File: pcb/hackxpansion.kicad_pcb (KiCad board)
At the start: 2 copper layers, 51 parts, among them IC1 ADS7128IRTET, J1 Conn_01x03_MountingPin, J3 USB_C_Receptacle_USB2.0_14P, J4 USB_C_Receptacle_USB2.0_14P, Q1 BSS138, Q2 2N7002, SW1 SW_Push, SW2 SW_Push, SW25 SW_On_Off, U12 BQ24075RGT, U2 RP2354B, U7 SPX3819M5-L-3-3, Y1 ABM8-272-T3

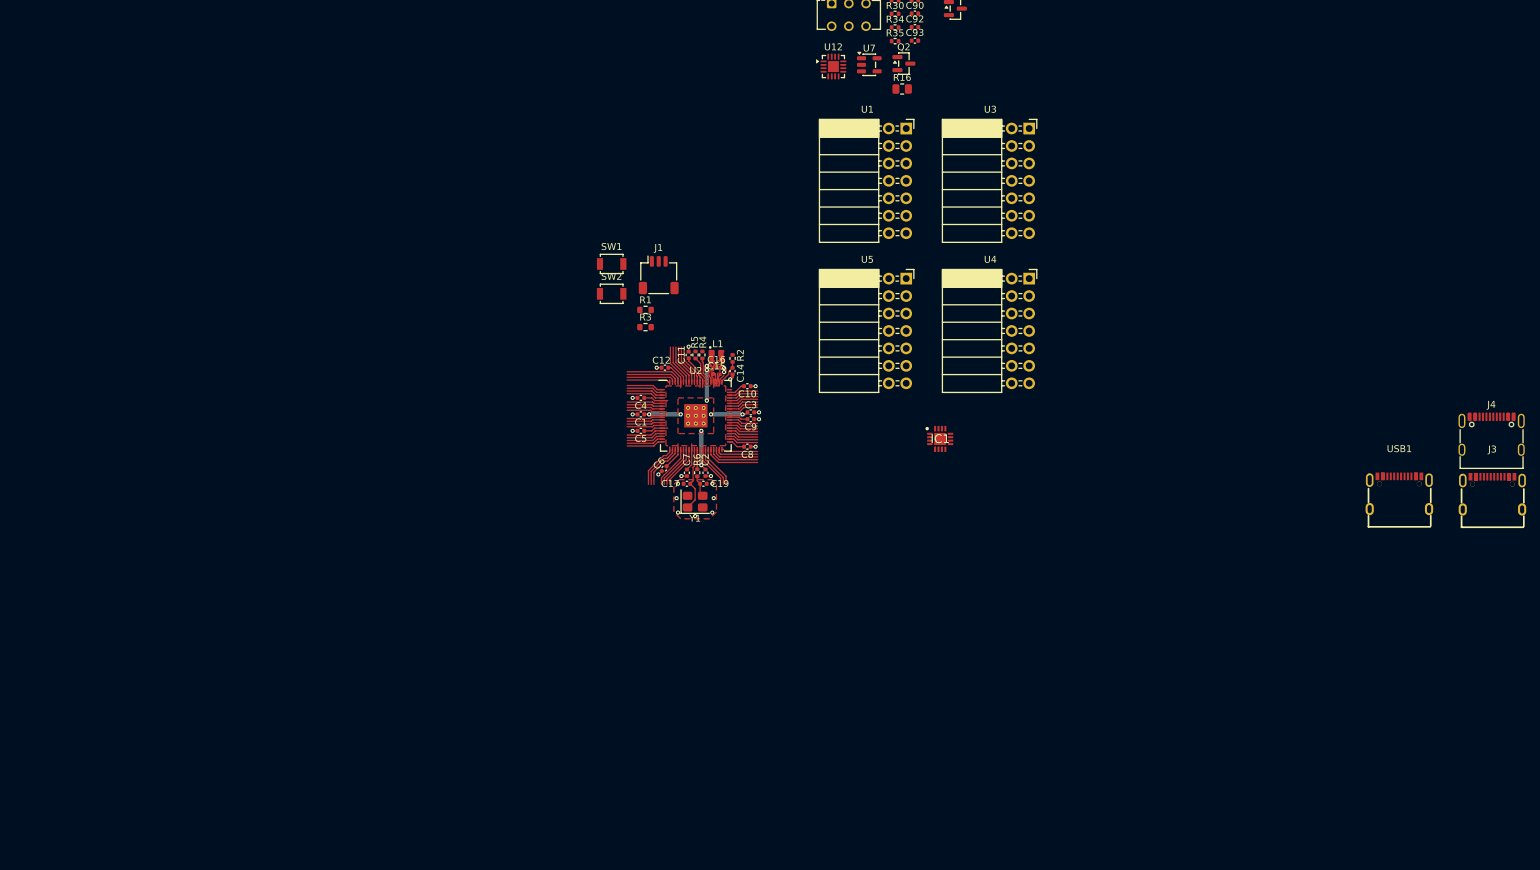
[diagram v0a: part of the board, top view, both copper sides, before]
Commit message: switched to pico blade connectors
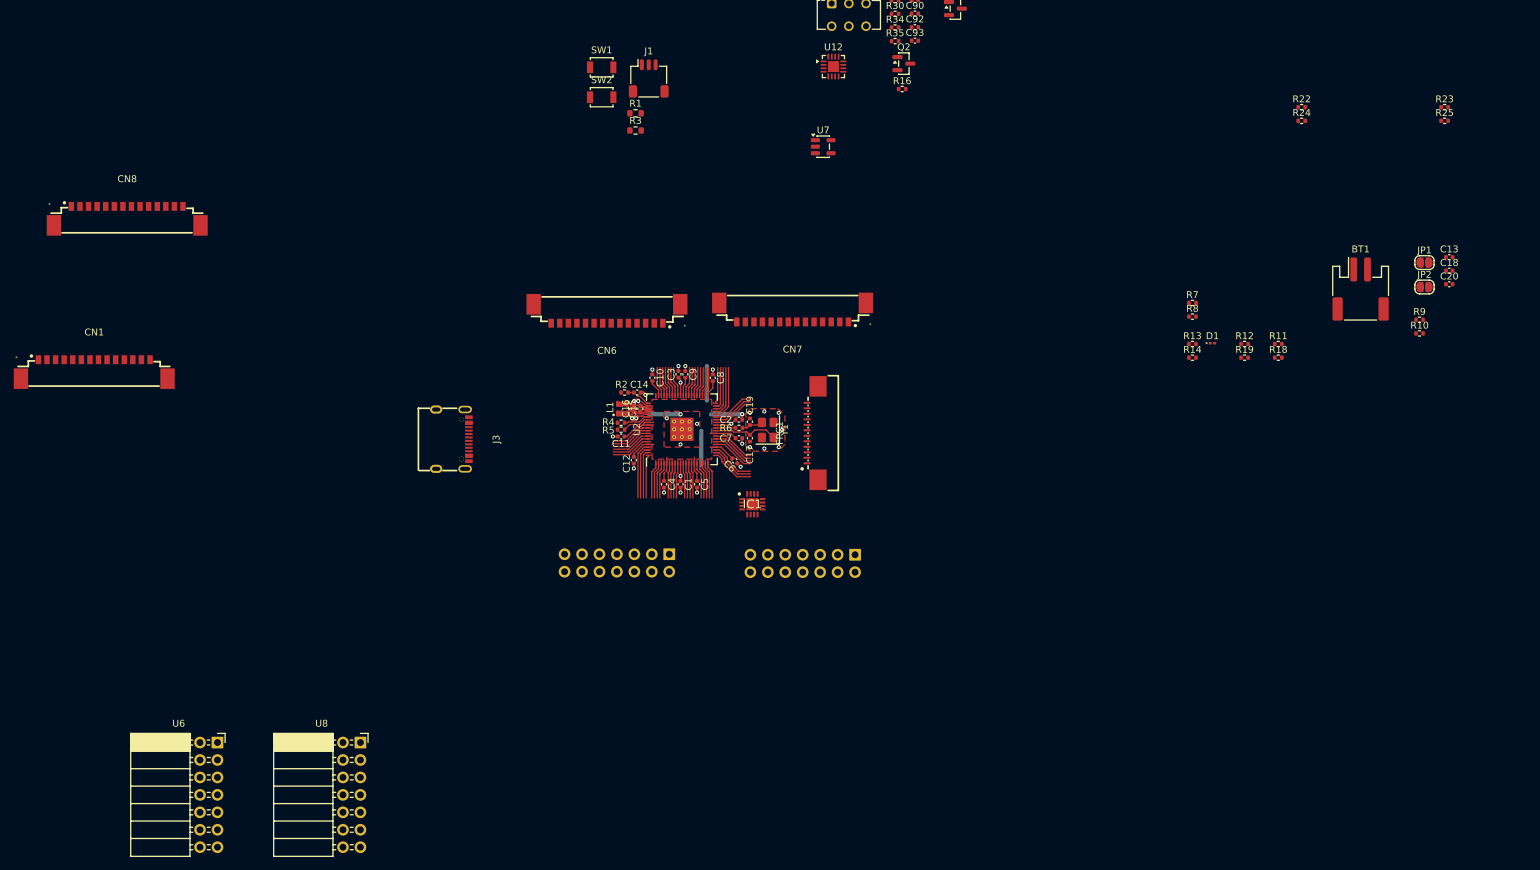
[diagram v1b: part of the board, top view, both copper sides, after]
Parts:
- removed J4: USB_C_Receptacle_USB2.0_14P, Connector_USB:USB_C_Receptacle_G-Switch_GT-USB-7010ASV
- removed U4, U5: ~, Connector_PinSocket_2.54mm:PinSocket_2x07_P2.54mm_Horizontal
- removed USB1: TYPE-C 16PIN 2MD, easyeda2kicad:USB-C-SMD_TYPE-C-16PIN-2MD-073
- added BT1: Battery_Cell, Connector_JST:JST_PH_S2B-PH-SM4-TB_1x02-1MP_P2.00mm_Horizontal, F.Cu at (225.8, 66.6)
- added C13: 1u, Capacitor_SMD:C_0402_1005Metric, F.Cu at (238.7, 61.9)
- added C18: 1u, Capacitor_SMD:C_0402_1005Metric, F.Cu at (238.7, 63.9)
- added C20: 1u, Capacitor_SMD:C_0402_1005Metric, F.Cu at (238.7, 65.9)
- added CN1: 533981471, easyeda2kicad:CONN-SMD_14P-P1.25_MOLEX_533981471, F.Cu at (41.4, 78.2)
- added CN6: 533981471, easyeda2kicad:CONN-SMD_14P-P1.25_MOLEX_533981471, F.Cu at (116.1, 70.2)
- added CN7: 533981471, easyeda2kicad:CONN-SMD_14P-P1.25_MOLEX_533981471, F.Cu at (143.1, 70.0)
- added CN8: 533981471, easyeda2kicad:CONN-SMD_14P-P1.25_MOLEX_533981471, F.Cu at (46.2, 55.9)
- added D1: LED, LED_SMD:LED_0201_0603Metric, F.Cu at (204.2, 74.4)
- added FPC1: AFC08-S12ECA-00, easyeda2kicad:FPC-SMD_AFC08-S12ECA-00, F.Cu at (146.0, 87.5)
- added JP1: SolderJumper_2_Open, Jumper:SolderJumper-2_P1.3mm_Open_RoundedPad1.0x1.5mm, F.Cu at (235.1, 62.7)
- added JP2: SolderJumper_2_Open, Jumper:SolderJumper-2_P1.3mm_Open_RoundedPad1.0x1.5mm, F.Cu at (235.1, 66.3)
- added R10: 5k1, Resistor_SMD:R_0402_1005Metric, F.Cu at (234.4, 73.0)
- added R11: 10K, Resistor_SMD:R_0402_1005Metric, F.Cu at (213.8, 74.6)
- added R12: 10K, Resistor_SMD:R_0402_1005Metric, F.Cu at (208.9, 74.6)
- added R13: 100R, Resistor_SMD:R_0402_1005Metric, F.Cu at (201.3, 74.6)
- added R14: 10k, Resistor_SMD:R_0402_1005Metric, F.Cu at (201.3, 76.5)
- added R18: 10K, Resistor_SMD:R_0402_1005Metric, F.Cu at (213.8, 76.5)
- added R19: 10K, Resistor_SMD:R_0402_1005Metric, F.Cu at (208.9, 76.5)
- added R22: 10K, Resistor_SMD:R_0402_1005Metric, F.Cu at (217.2, 40.1)
- added R23: 10K, Resistor_SMD:R_0402_1005Metric, F.Cu at (238.0, 40.1)
- added R24: 10K, Resistor_SMD:R_0402_1005Metric, F.Cu at (217.2, 42.1)
- added R25: 10K, Resistor_SMD:R_0402_1005Metric, F.Cu at (238.0, 42.1)
- added R7: 10, Resistor_SMD:R_0402_1005Metric, F.Cu at (201.3, 68.6)
- added R8: 10k, Resistor_SMD:R_0402_1005Metric, F.Cu at (201.3, 70.6)
- added R9: 5k1, Resistor_SMD:R_0402_1005Metric, F.Cu at (234.4, 71.0)
- added U6: ~, Connector_PinSocket_2.54mm:PinSocket_2x07_P2.54mm_Horizontal, F.Cu at (59.4, 132.6)
- added U8: ~, Connector_PinSocket_2.54mm:PinSocket_2x07_P2.54mm_Horizontal, F.Cu at (80.2, 132.6)
- C15, C16: footprint RP2354B_MINIMAL:C_0402_1005Metric_small_pads -> Capacitor_SMD:C_0402_1005Metric
- R16: footprint Resistor_SMD:R_0805_2012Metric -> Resistor_SMD:R_0402_1005Metric
- U1, U3: moved to B.Cu
- moved J3 151.6 mm to (93.6, 88.4), turned to -90 degrees
- moved U1 70.9 mm to (125.1, 105.2), turned to 90 degrees
- moved U3 67.0 mm to (152.2, 105.2), turned to 90 degrees
- moved IC1 28.9 mm to (137.2, 97.9)
- moved J1 28.7 mm to (122.1, 35.9)
- moved R1 28.7 mm to (120.2, 41.0)
- moved SW1 28.7 mm to (115.3, 34.3)
- moved SW2 28.7 mm to (115.3, 38.6)
- moved R3 28.7 mm to (120.2, 43.5)
- moved R2 16.5 mm to (118.6, 81.6), turned to 0 degrees
- moved L1 15.7 mm to (118.3, 84.0), turned to 90 degrees
- moved C11 15.4 mm to (118.1, 88.0), turned to 180 degrees
- moved R4 15.4 mm to (118.1, 86.0), turned to 0 degrees
- moved R5 15.3 mm to (118.1, 87.0), turned to 0 degrees
- moved Y1 14.8 mm to (139.5, 87.1), turned to 90 degrees
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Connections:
- net /ADC/i2c0.SCL renamed /Main Board/ADC/i2c0.SCL
- net /ADC/i2c0.SDA renamed /Main Board/ADC/i2c0.SDA
- net /Power/+BATT renamed /Main Board/Power/+BATT
- net /Power/ILIM renamed /Main Board/Power/ILIM
- net /Power/ISET renamed /Main Board/Power/ISET
- net /Power/REG-OUT renamed /Main Board/Power/REG-OUT
- net /Power/SYSOFF renamed /Main Board/Power/SYSOFF
- net /Power/TS renamed /Main Board/Power/TS
- net /Power/VSW renamed /Main Board/Power/VSW
- net /RP2354B/GPIO14 renamed /Main Board/ADC/SCL
- net /RP2354B/GPIO15 renamed /Main Board/ADC/SDA
- net /RP2354B/GPIO34 renamed /Main Board/RP2354B/spi.SCLK
- net /RP2354B/GPIO35 renamed /Main Board/RP2354B/spi.MOSI
- net /RP2354B/QSPI_SS renamed /Main Board/RP2354B/QSPI_SS
- net /RP2354B/RUN renamed /Main Board/RP2354B/RUN
- net /RP2354B/SWCLK renamed /Main Board/RP2354B/SWCLK
- net /RP2354B/SWDIO renamed /Main Board/RP2354B/SWDIO
- net /RP2354B/~{USB_BOOT} renamed /Main Board/RP2354B/~{USB_BOOT}
- C1 pad 2: GND -> /GND
- C10 pad 1: +3V3 -> /+3V3
- C10 pad 2: GND -> /GND
- C11 pad 1: +3V3 -> /+3V3
- C11 pad 2: GND -> /GND
- C12 pad 1: +3V3 -> /+3V3
- C12 pad 2: GND -> /GND
- C14 pad 2: GND -> /GND
- C15 pad 1: +3V3 -> /+3V3
- C15 pad 2: GND -> /GND
- C16 pad 2: GND -> /GND
- C17 pad 1: GND -> /GND
- C19 pad 1: GND -> /GND
- C2 pad 2: GND -> /GND
- C3 pad 2: GND -> /GND
- C4 pad 1: +3V3 -> /+3V3
- C4 pad 2: GND -> /GND
- C5 pad 1: +3V3 -> /+3V3
- C5 pad 2: GND -> /GND
- C6 pad 1: +3V3 -> /+3V3
- C6 pad 2: GND -> /GND
- C7 pad 1: +3V3 -> /+3V3
- C7 pad 2: GND -> /GND
- C8 pad 1: +3V3 -> /+3V3
- C8 pad 2: GND -> /GND
- C88 pad 1: GND -> /Main Board/Power/GND
- C88 pad 2: VBUS -> /Main Board/Power/VBUS
- C9 pad 1: +3V3 -> /+3V3
- C9 pad 2: GND -> /GND
- C90 pad 1: GND -> /Main Board/Power/GND
- C92 pad 1: GND -> /Main Board/Power/GND
- C93 pad 1: GND -> /Main Board/Power/GND
- C93 pad 2: /Power/3V3 -> /+3V3
- IC1 pad 1: /ADC/mod1.MD0 -> /Main Board/ADC/mod1.MD0
- IC1 pad 10: +3V3 -> /+3V3
- IC1 pad 12: /ADC/ALERT -> /Main Board/ADC/ALERT
- IC1 pad 15: /ADC/mod0.MD0 -> /Main Board/ADC/mod0.MD0
- IC1 pad 16: /ADC/mod0.MD1 -> /Main Board/ADC/mod0.MD1
- IC1 pad 17: GND -> /GND
- IC1 pad 2: /ADC/mod1.MD1 -> /Main Board/ADC/mod1.MD1
- IC1 pad 3: /ADC/mod2.MD0 -> /Connector Main Mod2/mod.MD0
- IC1 pad 4: /ADC/mod2.MD1 -> /Connector Main Mod2/mod.MD1
- IC1 pad 5: /ADC/mod3.MD0 -> /Connector Main Mod3/mod.MD0
- IC1 pad 6: /ADC/mod3.MD1 -> /Connector Main Mod3/mod.MD1
- IC1 pad 7: +3V3 -> /+3V3
- IC1 pad 9: GND -> /GND
- J1 pad 2: GND -> /GND
- J1 pad MP: GND -> /GND
- J3 pad A1: GND -> /GND
- J3 pad A12: GND -> /GND
- J3 pad A4: /USB/VBUS -> /Main Board/Power/VBUS
- J3 pad A5: /USB/CC1 -> /Main Board/USB/CC1
- J3 pad A6: /USB/D+ -> /Main Board/RP2354B/D+
- J3 pad A7: /USB/D- -> /Main Board/RP2354B/D-
- J3 pad A9: /USB/VBUS -> /Main Board/Power/VBUS
- J3 pad B1: GND -> /GND
- J3 pad B12: GND -> /GND
- J3 pad B4: /USB/VBUS -> /Main Board/Power/VBUS
- J3 pad B5: /USB/CC2 -> /Main Board/USB/CC2
- J3 pad B6: /USB/D+ -> /Main Board/RP2354B/D+
- J3 pad B7: /USB/D- -> /Main Board/RP2354B/D-
- J3 pad B9: /USB/VBUS -> /Main Board/Power/VBUS
- Q1 pad 1: /Display/BACKLIGHT -> /Main Board/Display/BACKLIGHT
- Q1 pad 2: GND -> /GND
- Q2 pad 2: GND -> /Main Board/Power/GND
- R2 pad 1: +3V3 -> /+3V3
- R28 pad 2: GND -> /Main Board/Power/GND
- R30 pad 2: GND -> /Main Board/Power/GND
- R34 pad 2: GND -> /Main Board/Power/GND
- R4 pad 1: /RP2354B/D- -> /Main Board/RP2354B/D-
- R5 pad 1: /RP2354B/D+ -> /Main Board/RP2354B/D+
- SW1 pad 1: GND -> /GND
- SW2 pad 1: GND -> /GND
- SW25 pad 1: GND -> /Main Board/Power/GND
- U1 pad 1: GND -> /GND
- U1 pad 10: /Module Bay 0/GPIO5 -> /Main Board/Module Bay 0/GPIO5
- U1 pad 11: /Module Bay 0/GPIO6 -> /Main Board/Module Bay 0/GPIO6
- U1 pad 12: /Module Bay 0/GPIO7 -> /Main Board/Module Bay 0/GPIO7
- U1 pad 13: /Module Bay 0/GPIO8 -> /Main Board/Module Bay 0/GPIO8
- U1 pad 14: /Module Bay 0/GPIO9 -> /Main Board/Module Bay 0/GPIO9
- U1 pad 2: +3V3 -> /+3V3
- U1 pad 3: /Module Bay 0/mod.MD0 -> /Main Board/ADC/mod0.MD0
- U1 pad 4: /Module Bay 0/mod.MD1 -> /Main Board/ADC/mod0.MD1
- U1 pad 5: /Module Bay 0/GPIO0 -> /Main Board/Module Bay 0/GPIO0
- U1 pad 6: /Module Bay 0/GPIO1 -> /Main Board/Module Bay 0/GPIO1
- U1 pad 7: /Module Bay 0/GPIO2 -> /Main Board/Module Bay 0/GPIO2
- U1 pad 8: /Module Bay 0/GPIO3 -> /Main Board/Module Bay 0/GPIO3
- U1 pad 9: /Module Bay 0/GPIO4 -> /Main Board/Module Bay 0/GPIO4
- U12 pad 13: VBUS -> /Main Board/Power/VBUS
- U12 pad 17: GND -> /Main Board/Power/GND
- U12 pad 4: GND -> /Main Board/Power/GND
- U12 pad 5: GND -> /Main Board/Power/GND
- U12 pad 8: GND -> /Main Board/Power/GND
- U2 pad 1: /RP2354B/GPIO4 -> /Main Board/Module Bay 0/GPIO3
- U2 pad 11: /RP2354B/GPIO12 -> /Main Board/Module Bay 1/GPIO3
- U2 pad 12: /RP2354B/GPIO13 -> /Main Board/Module Bay 1/GPIO0
- U2 pad 15: +3V3 -> /+3V3
- U2 pad 16: /RP2354B/GPIO16 -> /Main Board/Module Bay 1/GPIO1
- U2 pad 17: /RP2354B/GPIO17 -> /Main Board/Module Bay 1/GPIO9
- U2 pad 18: /RP2354B/GPIO18 -> /Connector Main Mod2/bank.GPIO1
- U2 pad 19: /RP2354B/GPIO19 -> /Connector Main Mod2/bank.GPIO0
- U2 pad 2: /RP2354B/GPIO5 -> /Main Board/ADC/ALERT
- U2 pad 20: /RP2354B/GPIO20 -> /Main Board/Module Bay 1/GPIO5
- U2 pad 21: /RP2354B/GPIO21 -> /Main Board/Module Bay 1/GPIO6
- U2 pad 22: /RP2354B/GPIO22 -> /Connector Main Mod2/bank.GPIO2
- U2 pad 23: /RP2354B/GPIO23 -> /Connector Main Mod2/bank.GPIO4
- U2 pad 24: +3V3 -> /+3V3
- U2 pad 25: /RP2354B/GPIO24 -> /Connector Main Mod3/bank.GPIO3
- U2 pad 26: /RP2354B/GPIO25 -> /Main Board/Display/DC
- U2 pad 27: /RP2354B/GPIO26 -> /Connector Main Mod2/bank.GPIO9
- U2 pad 28: /RP2354B/GPIO27 -> /Connector Main Mod3/bank.GPIO4
- U2 pad 29: +3V3 -> /+3V3
- U2 pad 3: /RP2354B/GPIO6 -> /Main Board/Module Bay 0/GPIO1
- U2 pad 36: /RP2354B/GPIO28 -> /Connector Main Mod2/bank.GPIO5
- U2 pad 37: /RP2354B/GPIO29 -> /Connector Main Mod2/bank.GPIO6
- U2 pad 38: /RP2354B/GPIO30 -> /Connector Main Mod3/bank.GPIO2
- U2 pad 39: /RP2354B/GPIO31 -> /Main Board/Display/BACKLIGHT
- U2 pad 4: /RP2354B/GPIO7 -> /Main Board/Module Bay 0/GPIO0
- U2 pad 40: /RP2354B/GPIO32 -> /Connector Main Mod2/bank.GPIO3
- U2 pad 41: +3V3 -> /+3V3
- U2 pad 42: /RP2354B/GPIO33 -> /Main Board/Module Bay 0/GPIO9
- U2 pad 45: /RP2354B/GPIO36 -> /Connector Main Mod3/bank.GPIO1
- U2 pad 46: /RP2354B/GPIO37 -> /Connector Main Mod3/bank.GPIO0
- U2 pad 47: /RP2354B/GPIO38 -> /Main Board/Display/CS
- U2 pad 48: /RP2354B/GPIO39 -> /Connector Main Mod3/bank.GPIO9
- U2 pad 49: /RP2354B/GPIO40 -> /Main Board/Module Bay 0/GPIO7
- U2 pad 5: +3V3 -> /+3V3
- U2 pad 50: +3V3 -> /+3V3
- U2 pad 52: /RP2354B/GPIO41 -> /Main Board/Module Bay 0/GPIO8
- U2 pad 53: /RP2354B/GPIO42 -> /Main Board/Module Bay 1/GPIO7
- U2 pad 54: /RP2354B/GPIO43 -> /Main Board/Module Bay 1/GPIO8
- U2 pad 55: /RP2354B/GPIO44 -> /Connector Main Mod2/bank.GPIO7
- U2 pad 56: /RP2354B/GPIO45 -> /Connector Main Mod2/bank.GPIO8
- U2 pad 57: /RP2354B/GPIO46 -> /Connector Main Mod3/bank.GPIO7
- U2 pad 58: /RP2354B/GPIO47 -> /Connector Main Mod3/bank.GPIO8
- U2 pad 59: +3V3 -> /+3V3
- U2 pad 6: /RP2354B/GPIO8 -> /Connector Main Mod3/bank.GPIO6
- U2 pad 60: +3V3 -> /+3V3
- U2 pad 62: GND -> /GND
- U2 pad 64: +3V3 -> /+3V3
- U2 pad 68: +3V3 -> /+3V3
- U2 pad 69: +3V3 -> /+3V3
- U2 pad 7: /RP2354B/GPIO9 -> /Connector Main Mod3/bank.GPIO5
- U2 pad 70: /RP2354B/QSPI_SD3 -> unconnected-(U2-QSPI_SD3-Pad70)
- U2 pad 71: /RP2354B/QSPI_SCLK -> unconnected-(U2-QSPI_SCLK-Pad71)
- U2 pad 72: /RP2354B/QSPI_SD0 -> /Main Board/Display/RESET
- U2 pad 73: /RP2354B/QSPI_SD2 -> unconnected-(U2-QSPI_SD2-Pad73)
- U2 pad 74: /RP2354B/QSPI_SD1 -> unconnected-(U2-QSPI_SD1-Pad74)
- U2 pad 76: +3V3 -> /+3V3
- U2 pad 77: /RP2354B/GPIO0 -> /Main Board/Module Bay 0/GPIO5
- U2 pad 78: /RP2354B/GPIO1 -> /Main Board/Module Bay 0/GPIO6
- U2 pad 79: /RP2354B/GPIO2 -> /Main Board/Module Bay 0/GPIO2
- U2 pad 8: /RP2354B/GPIO10 -> /Main Board/Module Bay 1/GPIO2
- U2 pad 80: /RP2354B/GPIO3 -> /Main Board/Module Bay 0/GPIO4
- U2 pad 81: GND -> /GND
- U2 pad 9: /RP2354B/GPIO11 -> /Main Board/Module Bay 1/GPIO4
- U3 pad 1: GND -> /GND
- U3 pad 10: /Module Bay 1/GPIO5 -> /Main Board/Module Bay 1/GPIO5
- U3 pad 11: /Module Bay 1/GPIO6 -> /Main Board/Module Bay 1/GPIO6
- U3 pad 12: /Module Bay 1/GPIO7 -> /Main Board/Module Bay 1/GPIO7
- U3 pad 13: /Module Bay 1/GPIO8 -> /Main Board/Module Bay 1/GPIO8
- U3 pad 14: /Module Bay 1/GPIO9 -> /Main Board/Module Bay 1/GPIO9
- U3 pad 2: +3V3 -> /+3V3
- U3 pad 3: /Module Bay 1/mod.MD0 -> /Main Board/ADC/mod1.MD0
- U3 pad 4: /Module Bay 1/mod.MD1 -> /Main Board/ADC/mod1.MD1
- U3 pad 5: /Module Bay 1/GPIO0 -> /Main Board/Module Bay 1/GPIO0
- U3 pad 6: /Module Bay 1/GPIO1 -> /Main Board/Module Bay 1/GPIO1
- U3 pad 7: /Module Bay 1/GPIO2 -> /Main Board/Module Bay 1/GPIO2
- U3 pad 8: /Module Bay 1/GPIO3 -> /Main Board/Module Bay 1/GPIO3
- U3 pad 9: /Module Bay 1/GPIO4 -> /Main Board/Module Bay 1/GPIO4
- U7 pad 2: GND -> /Main Board/Power/GND
- U7 pad 5: /Power/3V3 -> /+3V3
- Y1 pad 2: GND -> /GND
- Y1 pad 4: GND -> /GND
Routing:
- net +3V3: track 34.3 -> 0.00 mm
- net /+3V3: track 0.00 -> 34.3 mm
- net /GND: track 0.00 -> 14.3 mm, vias 0 -> 13
- net GND: track 9.67 -> 0.00 mm, vias 22 -> 0
- net /RP2354B/GPIO0: track 8.38 -> 0.00 mm
- net /Main Board/Module Bay 0/GPIO5: track 0.00 -> 8.38 mm
- net /RP2354B/GPIO28: track 8.06 -> 0.00 mm
- net /Connector Main Mod2/bank.GPIO5: track 0.00 -> 8.06 mm
- net /RP2354B/GPIO1: track 7.75 -> 0.00 mm
- net /Main Board/Module Bay 0/GPIO6: track 0.00 -> 7.75 mm
- net /RP2354B/GPIO29: track 7.43 -> 0.00 mm
- net /Connector Main Mod2/bank.GPIO6: track 0.00 -> 7.43 mm
- net /RP2354B/GPIO2: track 7.12 -> 0.00 mm
- net /Main Board/Module Bay 0/GPIO2: track 0.00 -> 7.12 mm
- net /RP2354B/GPIO30: track 6.81 -> 0.00 mm
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- added copper zone on F.Cu, net (none)
- removed copper zone on F.Cu, net +3V3
- removed copper zone on F.Cu, net GND

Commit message: reanottad stuff
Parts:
- removed C88, C90, C92, C93: 4u7, Capacitor_SMD:C_0402_1005Metric
- removed CN6, CN7, CN8: 533981471, easyeda2kicad:CONN-SMD_14P-P1.25_MOLEX_533981471
- removed J3: USB_C_Receptacle_USB2.0_14P, easyeda2kicad:USB-C-SMD_TYPE-C-16PIN-2MD-073
- removed R28: 3k9, Resistor_SMD:R_0402_1005Metric
- removed R30: 1k5, Resistor_SMD:R_0402_1005Metric
- removed R34, R35: 10k, Resistor_SMD:R_0402_1005Metric
- removed SW25: SW_On_Off, Button_Switch_THT:SW_CK_JS202011AQN_DPDT_Angled
- removed U12: BQ24075RGT, Package_DFN_QFN:VQFN-16-1EP_3x3mm_P0.5mm_EP1.6x1.6mm
- removed U8: ~, Connector_PinSocket_2.54mm:PinSocket_2x07_P2.54mm_Horizontal
- added C21: 4u7, Capacitor_SMD:C_0402_1005Metric, F.Cu at (94.2, 39.3)
- added C22: 4u7, Capacitor_SMD:C_0402_1005Metric, F.Cu at (94.2, 41.2)
- added C23: 4u7, Capacitor_SMD:C_0402_1005Metric, F.Cu at (94.2, 43.2)
- added C24: 4u7, Capacitor_SMD:C_0402_1005Metric, F.Cu at (94.2, 45.2)
- added CN2: 533981471, easyeda2kicad:CONN-SMD_14P-P1.25_MOLEX_533981471, F.Cu at (86.5, 78.9)
- added CN3: 533981471, easyeda2kicad:CONN-SMD_14P-P1.25_MOLEX_533981471, F.Cu at (86.5, 62.8)
- added CN4: 533981471, easyeda2kicad:CONN-SMD_14P-P1.25_MOLEX_533981471, F.Cu at (86.5, 70.8)
- added J2: USB_C_Receptacle_USB2.0_14P, easyeda2kicad:USB-C-SMD_TYPE-C-16PIN-2MD-073, F.Cu at (66.9, 63.6)
- added R15: 100k, Resistor_SMD:R_0402_1005Metric, F.Cu at (88.9, 47.3)
- added R17: 10K, Resistor_SMD:R_0402_1005Metric, F.Cu at (62.9, 72.2)
- added R20: 10K, Resistor_SMD:R_0402_1005Metric, F.Cu at (78.8, 39.3)
- added R21: 10K, Resistor_SMD:R_0402_1005Metric, F.Cu at (67.8, 72.2)
- added SW3: SW_On_Off, Button_Switch_THT:SW_CK_JS202011AQN_DPDT_Angled, F.Cu at (85.0, 39.8)
- added U4: ~, Connector_PinSocket_2.54mm:PinSocket_2x07_P2.54mm_Horizontal, F.Cu at (75.1, 40.6)
- added U5: SPX3819M5-L-3-3, Package_TO_SOT_SMD:SOT-23-5, F.Cu at (84.8, 48.7)
- R16: value 100k -> 10K
- R22: value 10K -> 3k9
- R23: value 10K -> 1k5
- R24, R25: value 10K -> 10k
- U7: value SPX3819M5-L-3-3 -> BQ24075RGT; footprint Package_TO_SOT_SMD:SOT-23-5 -> Package_DFN_QFN:VQFN-16-1EP_3x3mm_P0.5mm_EP1.6x1.6mm
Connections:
- FPC1 pad 13: /GND -> unconnected-(FPC1-Pad13)
- FPC1 pad 14: /GND -> unconnected-(FPC1-Pad14)
- R16 pad 1: /Main Board/Power/+BATT -> /Main Board/ADC/mod0.MD1
- R16 pad 2: Net-(SW25A-C) -> /GND
- R18 pad 1: /Main Board/ADC/mod0.MD1 -> /Connector Daughter Mod2/mod.MD1
- R19 pad 1: /Main Board/ADC/mod1.MD1 -> /Connector Daughter Mod3/mod.MD1
- R22 pad 1: /Connector Daughter Mod2/mod.MD1 -> /Main Board/Power/ISET
- R22 pad 2: /GND -> /Main Board/Power/GND
- R23 pad 1: /Connector Daughter Mod3/mod.MD1 -> /Main Board/Power/ILIM
- R23 pad 2: /GND -> /Main Board/Power/GND
- R24 pad 1: /Connector Daughter Mod2/mod.MD0 -> /Main Board/Power/TS
- R24 pad 2: /GND -> /Main Board/Power/GND
- R25 pad 1: /Connector Daughter Mod3/mod.MD0 -> Net-(D1-K)
- R25 pad 2: /GND -> Net-(U7-~{CHG})
- U6 pad 10: /Connector Daughter Mod2/bank.GPIO5 -> /Connector Daughter Mod3/bank.GPIO5
- U6 pad 11: /Connector Daughter Mod2/bank.GPIO6 -> /Connector Daughter Mod3/bank.GPIO6
- U6 pad 12: /Connector Daughter Mod2/bank.GPIO7 -> /Connector Daughter Mod3/bank.GPIO7
- U6 pad 13: /Connector Daughter Mod2/bank.GPIO8 -> /Connector Daughter Mod3/bank.GPIO8
- U6 pad 14: /Connector Daughter Mod2/bank.GPIO9 -> /Connector Daughter Mod3/bank.GPIO9
- U6 pad 3: /Connector Daughter Mod2/mod.MD0 -> /Connector Daughter Mod3/mod.MD0
- U6 pad 4: /Connector Daughter Mod2/mod.MD1 -> /Connector Daughter Mod3/mod.MD1
- U6 pad 5: /Connector Daughter Mod2/bank.GPIO0 -> /Connector Daughter Mod3/bank.GPIO0
- U6 pad 6: /Connector Daughter Mod2/bank.GPIO1 -> /Connector Daughter Mod3/bank.GPIO1
- U6 pad 7: /Connector Daughter Mod2/bank.GPIO2 -> /Connector Daughter Mod3/bank.GPIO2
- U6 pad 8: /Connector Daughter Mod2/bank.GPIO3 -> /Connector Daughter Mod3/bank.GPIO3
- U6 pad 9: /Connector Daughter Mod2/bank.GPIO4 -> /Connector Daughter Mod3/bank.GPIO4
- U7 pad 1: /Main Board/Power/REG-OUT -> /Main Board/Power/TS
- U7 pad 2: /Main Board/Power/GND -> /Main Board/Power/+BATT
- U7 pad 3: /Main Board/Power/REG-OUT -> /Main Board/Power/+BATT
- U7 pad 4: unconnected-(U7-BP-Pad4) -> /Main Board/Power/GND
- U7 pad 5: /+3V3 -> /Main Board/Power/GND

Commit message: moved stuff around
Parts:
- added A1: RaspberryPi_Pico, Module:RaspberryPi_Pico_Common_Unspecified, F.Cu at (219.5, 135.0)
- moved J1 68.7 mm to (147.3, 99.9), turned to 90 degrees
- moved U7 65.0 mm to (106.3, 96.0)
- moved CN1 59.7 mm to (-18.1, 82.6)
- moved CN3 58.4 mm to (144.2, 71.2), turned to 180 degrees
- moved CN4 55.8 mm to (30.8, 75.0)
- moved SW3 51.5 mm to (95.8, 90.1), turned to -90 degrees
- moved J2 32.8 mm to (95.1, 80.3), turned to -90 degrees
- moved CN2 30.9 mm to (116.5, 71.6), turned to 180 degrees

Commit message: updated some stuff on pcb
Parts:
- removed A1: RaspberryPi_Pico, Module:RaspberryPi_Pico_Common_Unspecified
- added J3: ~, Connector_PinHeader_2.54mm:PinHeader_2x07_P2.54mm_Horizontal, F.Cu at (567.8, 152.3)
- added J3: ~, Connector_PinHeader_2.54mm:PinHeader_2x07_P2.54mm_Horizontal, F.Cu at (631.8, 150.9)
- added J3: ~, Connector_PinHeader_2.54mm:PinHeader_2x07_P2.54mm_Horizontal, F.Cu at (541.3, 152.3)
- moved U1 80.9 mm to (68.9, 163.3)

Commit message: did some layout
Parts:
- removed the J3 at (567.8, 152.3)
- removed the J3 at (541.3, 152.3)
- added J3: ~, Connector_PinHeader_2.54mm:PinHeader_2x07_P2.54mm_Horizontal, F.Cu at (217.3, 137.3)
- added J3: ~, Connector_PinHeader_2.54mm:PinHeader_2x07_P2.54mm_Horizontal, F.Cu at (567.8, 152.8)
- added J3: ~, Connector_PinHeader_2.54mm:PinHeader_2x07_P2.54mm_Horizontal, F.Cu at (541.3, 152.8)
- added J3: ~, Connector_PinHeader_2.54mm:PinHeader_2x07_P2.54mm_Horizontal, F.Cu at (243.8, 137.3)
- BT1: footprint Connector_JST:JST_PH_S2B-PH-SM4-TB_1x02-1MP_P2.00mm_Horizontal -> Connector_Molex:Molex_PicoBlade_53261-0271_1x02-1MP_P1.25mm_Horizontal
- U1, U3: moved to F.Cu
- moved U1 155.1 mm to (217.3, 118.0)
- moved J2 121.9 mm to (215.6, 98.6)
- moved SW3 121.5 mm to (216.3, 106.1)
- moved U7 116.7 mm to (222.9, 95.2)
- moved FPC1 116.1 mm to (260.2, 108.5)
- moved J1 113.7 mm to (260.9, 96.3)
- moved C1 112.6 mm to (238.0, 112.6)
- moved C11 112.6 mm to (229.4, 105.6)
- moved C12 112.6 mm to (231.2, 109.1)
- moved C14 112.6 mm to (231.7, 99.2)
- moved C16 112.6 mm to (231.2, 101.6)
- moved C17 112.6 mm to (248.1, 105.9)
- moved C19 112.6 mm to (248.1, 103.5)
- moved C2 112.6 mm to (246.5, 103.2)
- moved C3 112.6 mm to (237.7, 96.6)
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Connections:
- BT1 pad 1: /Main Board/Power/+BATT -> /GND
- BT1 pad 2: /GND -> /Main Board/Power/+BATT
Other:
- board outline added: 376 x 59.8 mm
